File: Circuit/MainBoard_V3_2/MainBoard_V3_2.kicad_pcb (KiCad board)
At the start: 2 copper layers, 56 x 65 mm, 141 parts, among them J1 Conn_01x02, J10 Conn_01x03, J11 Conn_01x03, J12 Conn_01x04, J13 Conn_01x04, J14 Conn_01x04, J15 Conn_01x04, J2 Conn_01x02, J3 Conn_01x02, J4 Conn_01x04, J5 Conn_01x02, J6 Conn_01x02, J7 Conn_01x02, J8 Conn_01x07, J9 Raspberry_Pi_2_3, Q1 Q_PMOS_GDS, Q10 BSS138, Q2 Q_PMOS_GDS, Q3 BSS138, Q4 IRLML6402, Q5 BSS138, Q6 BSS138, Q7 BSS138, Q8 BSS138, Q9 BSS138, SW1 SW_Push, SW2 SW_Push, SW3 SW_Push, SW4 SW_Slide_DPDT, SW5 SW_Slide_DPDT, U1 STM32F446RETx, U2 LM1117MP-3.3, U3 MPU-6050, U4 INA180A2, U5 INA180A2, Y1 CSTNE16M0V530000R0

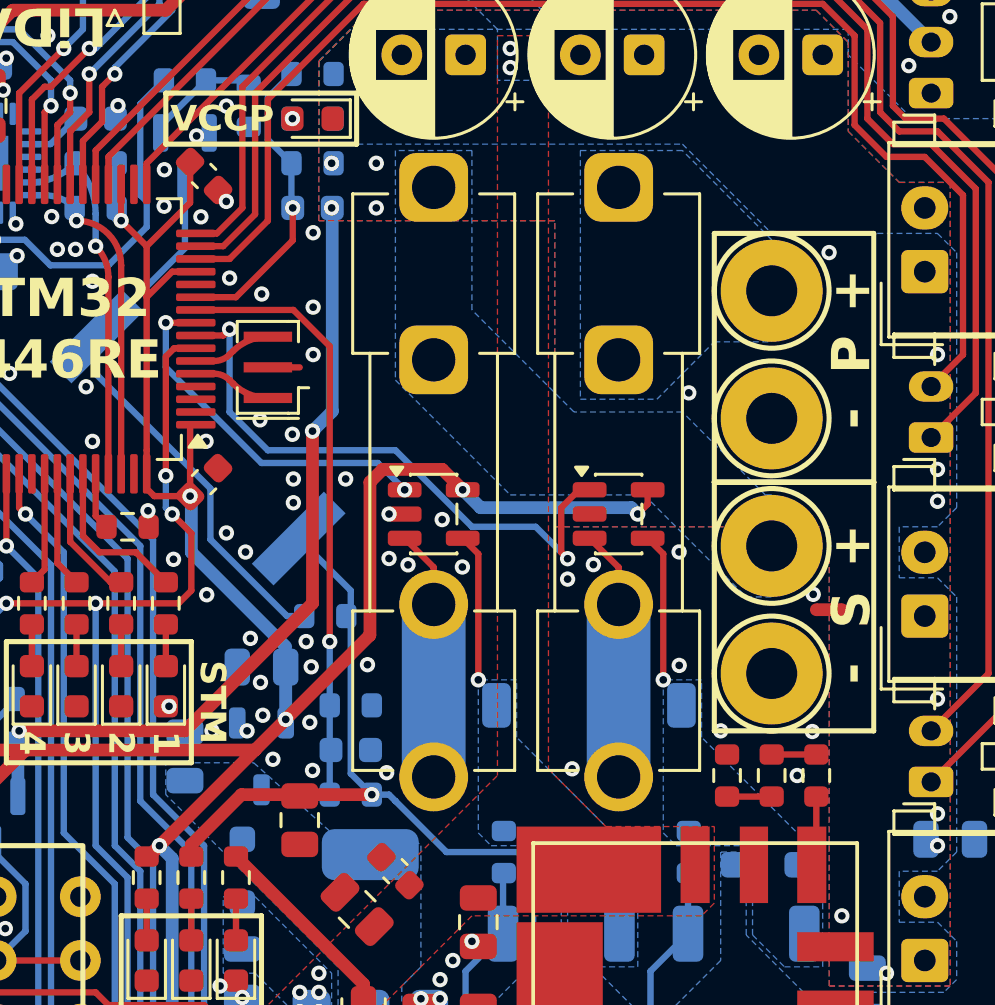
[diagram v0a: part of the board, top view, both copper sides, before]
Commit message: TVSダイオード追加
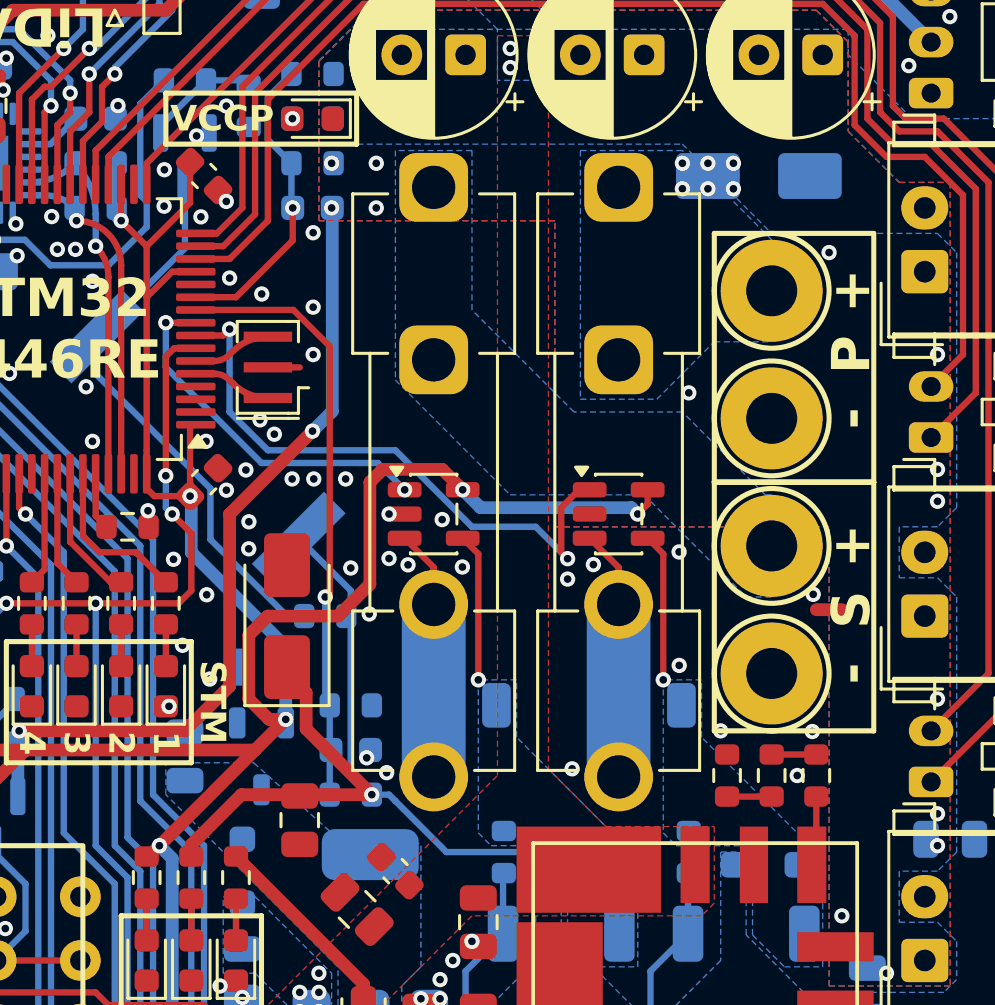
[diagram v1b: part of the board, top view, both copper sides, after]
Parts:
- added D17: SMAJ13A, Diode_SMD:D_SMA, B.Cu at (14.8, -15.0)
- added D18: SMAJ13A, Diode_SMD:D_SMA, F.Cu at (-3.75, 2.25)
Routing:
- net VCC: track 27.8 -> 34.2 mm
- net +3V3: track 222.1 -> 225.3 mm
- net GNDP: vias 16 -> 22
- net GND: vias 243 -> 239

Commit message: 修正多分最終
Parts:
- added C33: 1uf, Capacitor_SMD:C_0603_1608Metric, B.Cu at (19.5, -21.2)
- added C34: 1uf, Capacitor_SMD:C_0603_1608Metric, B.Cu at (4.75, 26.5)
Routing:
- net NRST: track 75.0 -> 75.8 mm
- net PC_TX: track 58.1 -> 58.9 mm
- net TX3: track 79.0 -> 79.8 mm
- net SWDIO: track 56.1 -> 57.0 mm
- net SWCLK: track 56.6 -> 57.4 mm
- net PC_RX: track 62.2 -> 63.0 mm
- net RX3: track 75.0 -> 75.8 mm
- net GNDP: vias 22 -> 27
- net GND: vias 239 -> 255

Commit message: rasとstmをプルアップで繋げた
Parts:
- added R45: 10k, Resistor_SMD:R_0603_1608Metric, B.Cu at (-19.2, -11.0)
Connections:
- J9 pad 31: unconnected-(J9-GCLK2/GPIO6-Pad31) -> RAS_SIG
- U1 pad 33: unconnected-(U1-PB12-Pad33) -> RAS_SIG
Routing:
- net RAS_SIG: track 0.00 -> 6.86 mm, vias 0 -> 1
- net +3V3: track 225.6 -> 227.9 mm
- net BTN2: track 27.8 -> 27.3 mm
- net GNDP: vias 27 -> 37
- net GND: vias 255 -> 258
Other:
- board text removed: "MPU6050"

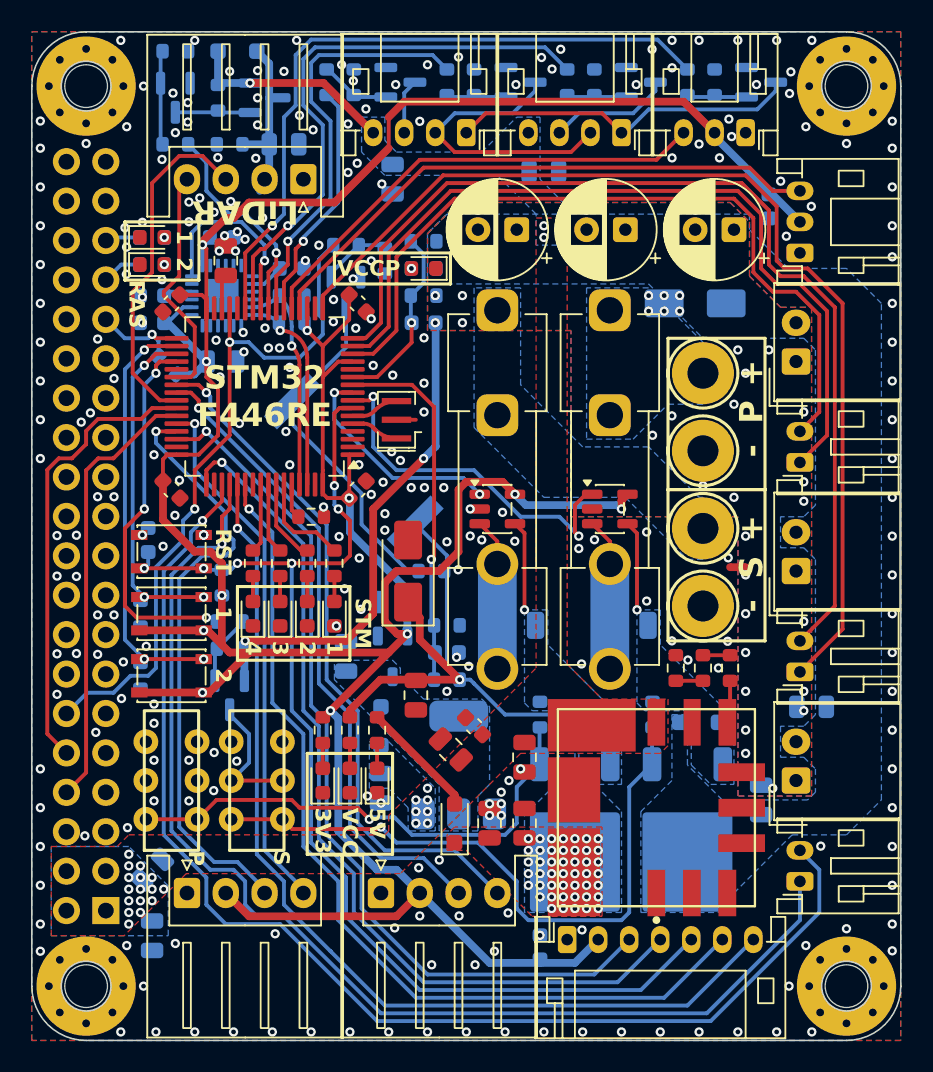
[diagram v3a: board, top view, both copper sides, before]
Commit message: ティアドロップ追加
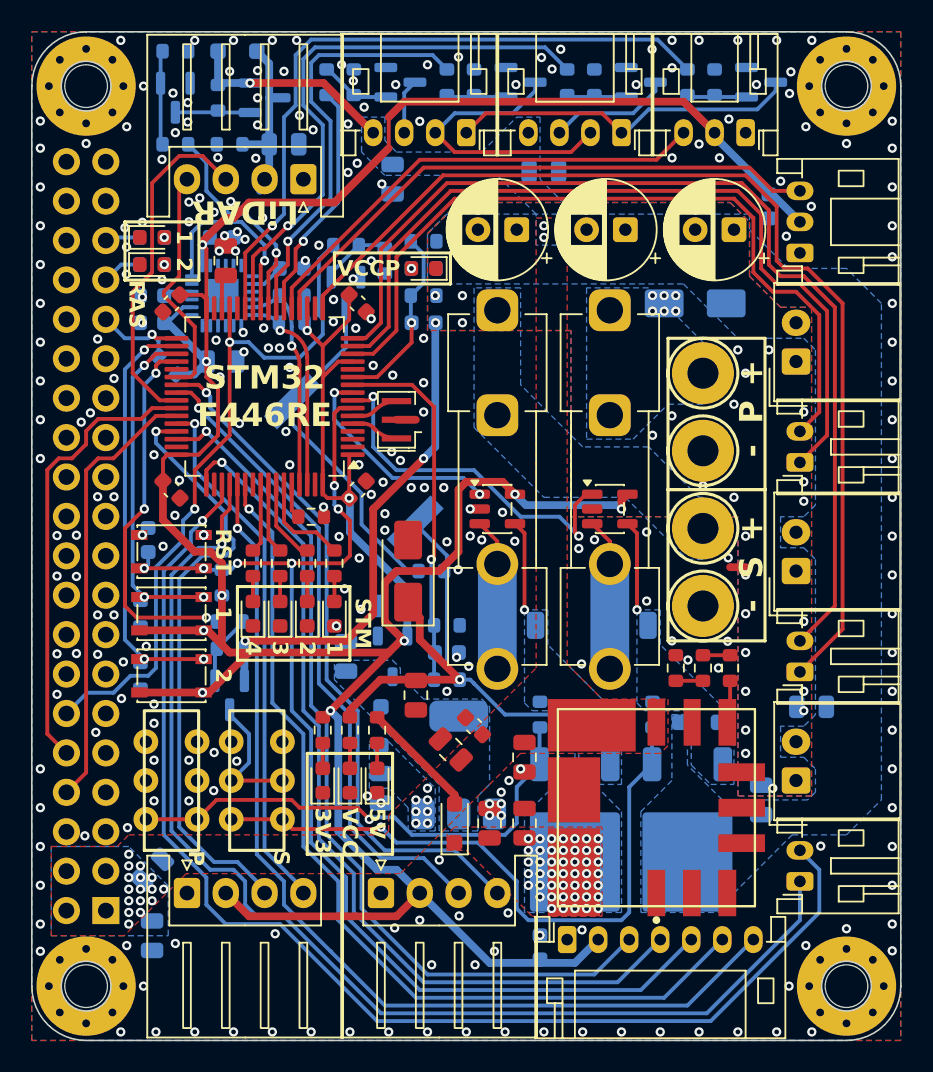
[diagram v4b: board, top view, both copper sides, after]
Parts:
- moved C19 0.25 mm to (-4.75, 4.50)

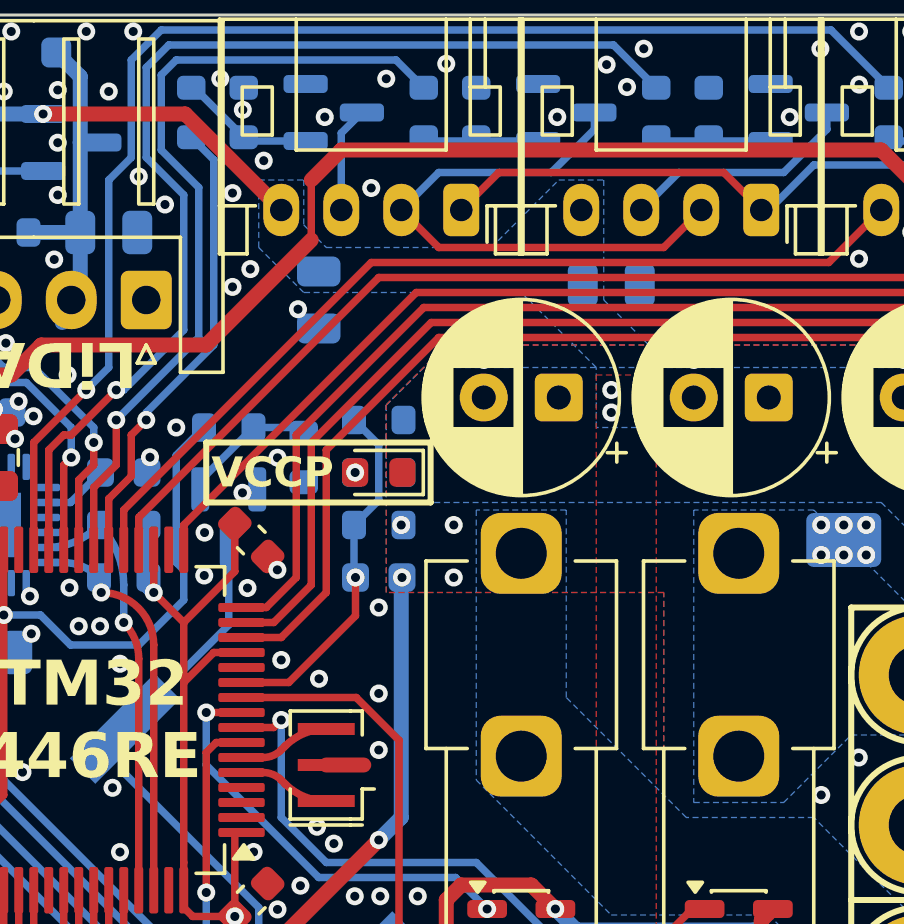
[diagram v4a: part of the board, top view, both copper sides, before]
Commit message: fableに聞いて修正（コンデンサ追加など）
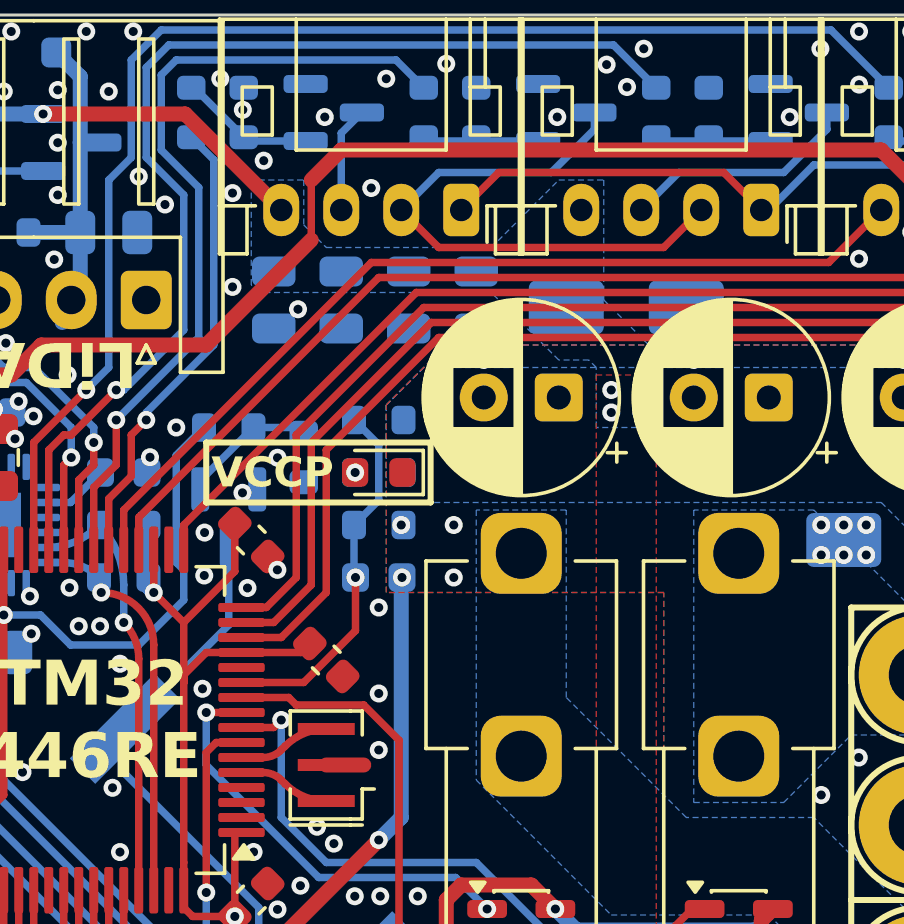
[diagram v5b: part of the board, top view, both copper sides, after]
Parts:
- added C35: 0.1uf, Capacitor_SMD:C_0603_1608Metric, F.Cu at (-4.50, -11.0)
- added C36: 10u, Capacitor_SMD:C_0805_2012Metric, B.Cu at (-1.75, -23.0)
- added C37: 10u, Capacitor_SMD:C_0805_2012Metric, B.Cu at (-6.25, -23.0)
- added D19: SMAJ5.0A, Diode_SMD:D_SMA, B.Cu at (5.50, -22.8)
- moved C4 4.53 mm to (0.50, -23.0), turned to -90 degrees
- moved C31 0.75 mm to (-4.00, -23.0)
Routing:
- net +3V3: track 228.0 -> 230.6 mm
- net GND: vias 258 -> 256
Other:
- board text removed: "LED"
